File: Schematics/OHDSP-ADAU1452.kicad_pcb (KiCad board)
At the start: 4 copper layers, 100 x 100 mm, 308 parts, among them CN201 COAX, CN401 COAX, CN402 COAX, CN405 COAX, CN406 COAX, P201 CONN_2x1, P202 CONN_2x1, P203 CONN_6X2, P204 CONN_6x1, P301 CONN_2x1, P302 CONN_2x1, P303 PIN, P304 PIN, P305 PIN, P306 PIN, P601 CONN_02X05, P602 CONN_02X05, P603 CONN_02X05, P604 CONN_02X05, P605 CONN_3x1, P606 CONN_6X2, P607 CONN_02X05, P608 CONN_02X05, P609 CONN_02X20, P610 CONN_02X05, P611 CONN_5x1, P613 CONN_02X05, P614 CONN_02X05, P615 CONN_02X05, P616 CONN_02X05, SW201 SWITCH, SW202 SWITCH, U201 ADAU1452WBCPZ, U202 ADM13307-5ARZ, U203 25AA1024, U301 IC-REG-XRP7659ISTR-F, U302 IC-REG-XRP7659ISTR-F, U304 IC-REG-XC6210B332MR, U305 IC-REG-XC6210B332MR, U401 NB3L553, U501 IC-SPDIF-RX-OPTO, U502 IC-SPDIF-TX-OPTO, X201 24M576

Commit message: PCB work
More pcb work, some footprint changes, previous commit also had some
minor footprint changes and 0R resistors added...
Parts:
- C239, C240, C243, C245, L204, L205, R228, R234: moved to B.Cu
- moved L205 438.1 mm to (233.7, 130.3)
- moved C240 426.7 mm to (239.5, 136.1), turned to 90 degrees
- moved L204 423.6 mm to (233.7, 137.7)
- moved C245 363.9 mm to (233.7, 132.8), turned to 180 degrees
- moved C239 353.0 mm to (233.7, 135.1), turned to 180 degrees
- moved R228 301.5 mm to (237.0, 136.1), turned to 90 degrees
- moved R234 295.6 mm to (237.0, 131.8), turned to 270 degrees
- moved C227 16.7 mm to (273.3, 99.1), turned to 0 degrees
- moved C243 15.6 mm to (239.5, 131.8), turned to 270 degrees
- moved C224 15.6 mm to (276.4, 102.1), turned to 90 degrees
- moved R225 15.3 mm to (275.6, 105.2)
- moved C225 15.1 mm to (273.3, 103.1), turned to 0 degrees
- moved C226 15.1 mm to (273.3, 101.1), turned to 0 degrees
- moved L203 11.8 mm to (271.0, 105.2), turned to 0 degrees
- moved C228 2.90 mm to (276.6, 88.1), turned to 180 degrees
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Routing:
- net /ADAU1452/DVDD: track 78.3 -> 93.8 mm, vias 1 -> 2
- net VPP: track 32.9 -> 37.6 mm
- net /ADAU1452/IOVDD: track 78.1 -> 78.3 mm, vias 1 -> 2

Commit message: PCB work, footprint changes
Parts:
- C239, C240, C243, C245, L204, L205, R228, R234: moved to F.Cu
- R217: footprint OHDSP-Footprints-Pretty:SMD-0805 -> OHDSP-Footprints-Pretty:SMD-0603
- R601, R602, R603, R634, R646, R647: moved to B.Cu
- moved C245 72.2 mm to (278.1, 75.9), turned to 270 degrees
- moved R234 68.4 mm to (275.3, 75.2), turned to 0 degrees
- moved L204 66.9 mm to (261.9, 77.0), turned to 270 degrees
- moved L205 66.9 mm to (271.5, 75.2)
- moved C243 65.5 mm to (275.3, 77.0), turned to 0 degrees
- moved R228 60.2 mm to (260.1, 80.5), turned to 180 degrees
- moved C240 59.4 mm to (262.9, 81.5), turned to 270 degrees
- moved C239 59.1 mm to (260.1, 82.3), turned to 0 degrees
- moved R603 22.4 mm to (294.9, 74.9)
- moved R602 21.6 mm to (297.4, 74.7)
- moved L203 18.8 mm to (252.7, 101.2)
- moved C225 18.1 mm to (255.7, 98.9)
- moved C241 17.0 mm to (286.2, 81.8)
- moved C226 16.6 mm to (256.7, 102.3)
- moved C250 16.2 mm to (289.1, 81.6)
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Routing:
- net /ADAU1452/IOVDD: track 78.3 -> 12.6 mm, vias 2 -> 0
- net VAA: track 0.00 -> 44.2 mm
- net VPP: track 37.6 -> 0.00 mm, vias 1 -> 0
- net (no net): track 23.4 -> 56.3 mm, vias 0 -> 1
- net /ADAU1452/DVDD: track 93.8 -> 68.5 mm, vias 2 -> 1
- net /ADAU1452/PVDD: track 6.94 -> 17.1 mm
- net /ADAU1452/AVDD: track 4.87 -> 13.0 mm
- net VDD: track 41.7 -> 48.6 mm
- net Net-(P609-Pad40): track 5.35 -> 0.00 mm
- net Net-(P609-Pad38): track 5.18 -> 0.00 mm
- net Net-(P609-Pad35): track 2.85 -> 0.03 mm
- net Net-(C221-Pad2): track 0.00 -> 1.52 mm
- net Net-(P609-Pad19): track 6.00 -> 4.85 mm

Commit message: PCB changes, minor schematic changes
Removed switch on selfboot pin, as it has a jumper anyway... Removed
SPI/I2C jumper for selfboot as sticking with serial EEPROM. Changed some
component footprints (R207 to R216 0603 to 0805).
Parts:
- removed C202: 100n, OHDSP-Footprints-Pretty:SMD-0805
- removed C248: 220u, OHDSP-Footprints-Pretty:CAP-TH-D6.3mmP2.5mm
- removed P202: CONN_2x1, OHDSP-Footprints-Pretty:CONN_SIL_2
- removed SW201: SWITCH, OHDSP-Footprints-Pretty:SW_TACT_TH
- R205: value 1k -> N/F
- R207, R208, R209, R210, R211, R212, R213, R214, R215, R216: footprint OHDSP-Footprints-Pretty:SMD-0603 -> OHDSP-Footprints-Pretty:SMD-0805
- R644: moved to B.Cu
- moved P201 471.7 mm to (259.7, 99.1), turned to 270 degrees
- moved R201 448.8 mm to (257.2, 101.3), turned to 90 degrees
- moved R216 43.4 mm to (253.5, 91.9)
- moved R211 43.4 mm to (257.3, 91.9)
- moved R214 41.6 mm to (248.2, 93.0)
- moved C226 37.9 mm to (284.0, 128.7)
- moved R215 37.6 mm to (251.5, 93.0), turned to 270 degrees
- moved R212 37.4 mm to (255.4, 93.0), turned to 270 degrees
- moved R213 36.3 mm to (248.2, 95.2)
- moved L203 35.3 mm to (276.5, 127.3)
- moved C227 35.1 mm to (276.6, 130.8)
- moved C225 34.4 mm to (270.1, 130.0)
- moved P610 17.6 mm to (240.0, 98.0), turned to 180 degrees
- moved R209 17.3 mm to (248.5, 104.5), turned to 0 degrees
- moved R210 13.0 mm to (248.5, 106.6)
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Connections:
- R205 pad 1: Net-(P202-Pad2) -> /ADAU1452/SS_M/MP0
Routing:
- net /ADAU1452/DVDD: track 68.5 -> 19.4 mm
- net Net-(P609-Pad24): track 0.00 -> 28.3 mm
- net Net-(P609-Pad19): track 4.85 -> 20.5 mm
- net Net-(R212-Pad2): track 6.53 -> 21.9 mm
- net Net-(P609-Pad21): track 16.3 -> 30.5 mm
- net Net-(R207-Pad2): track 10.9 -> 23.8 mm
- net /ADAU1452/SPI_MOSI: track 4.66 -> 17.3 mm
- net /ADAU1452/SELFBOOT: track 0.00 -> 12.4 mm
- net Net-(R211-Pad2): track 7.38 -> 19.5 mm
- net /ADAU1452/SPI_MISO: track 26.3 -> 16.7 mm
- net /ADAU1452/I2C_SCL: track 72.1 -> 63.2 mm
- net Net-(R209-Pad2): track 15.7 -> 24.0 mm
- net Net-(P607-Pad7): track 28.0 -> 21.3 mm
- net /ADAU1452/M_SS: track 47.4 -> 53.2 mm
- net /ADAU1452/XTALIN: track 26.0 -> 20.3 mm
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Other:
- rule trace_min: 0.25 -> 0.2

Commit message: PCB Work
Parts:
- added C202: 220u, OHDSP-Footprints-Pretty:CAP-TH-D6.3mmP2.5mm, F.Cu at (255.0, 81.0)
- moved L203 30.7 mm to (254.1, 106.2)
- moved R601 9.41 mm to (300.7, 76.7)
- moved R634 9.14 mm to (281.9, 76.6)
- moved R603 4.50 mm to (290.6, 76.2)
- moved R646 0.77 mm to (276.2, 75.8), turned to 270 degrees
- moved C507 0.51 mm to (288.0, 71.1)
- moved R647 0.40 mm to (278.6, 75.7), turned to 270 degrees
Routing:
- net (no net): track 56.3 -> 23.4 mm, vias 1 -> 0
- net /ADAU1452/ADAU_SPDIF_RX: track 19.8 -> 18.9 mm
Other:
- board text added: "Seeed Studio/Fusion PCB do a 1mm stackup that would give reasonable trace widths For 50ohm use inner layer as ground (5mil clearance), trace width is 0.24mm For 75ohm keep inner layers clear, bottom as ground, trace width is 0.5mm For 100ohm keep inner layers clear, bottom ground, use 0.25mm All are approximate..."

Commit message: PCB Work
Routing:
- net /ADAU1452/DACOUT_BCLK2: track 20.8 -> 13.9 mm
- net /ADAU1452/DACOUT_SDATA2: track 18.0 -> 11.8 mm

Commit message: PCB work, removed a cap
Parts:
- removed C402: 220u, OHDSP-Footprints-Pretty:CAP-TH-D6.3mmP2.5mm
- C321, C503, C504, C505, C506, R231, R502: moved to B.Cu
- moved C506 651.2 mm to (300.5, 61.5), turned to 180 degrees
- moved R502 649.4 mm to (297.9, 65.8), turned to 180 degrees
- moved C505 633.9 mm to (282.4, 61.5), turned to 180 degrees
- moved C503 630.3 mm to (277.6, 61.0), turned to 90 degrees
- moved C504 624.5 mm to (272.5, 61.0), turned to 90 degrees
- moved R501 621.8 mm to (270.3, 61.0), turned to 90 degrees
- moved C501 619.2 mm to (267.2, 59.9), turned to 180 degrees
- moved L501 618.4 mm to (267.2, 62.5)
- moved C502 599.5 mm to (275.1, 61.0), turned to 90 degrees
- moved C401 387.7 mm to (258.1, 107.2), turned to 270 degrees
- moved C403 385.6 mm to (255.1, 108.2)
- moved C404 383.4 mm to (252.7, 115.4), turned to 180 degrees
- moved L401 377.8 mm to (252.3, 105.0), turned to 270 degrees
- moved R401 370.8 mm to (255.3, 106.0)
- moved C225 47.4 mm to (269.0, 82.7)
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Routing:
- net /ADAU1452/DVDD: track 19.4 -> 87.7 mm, vias 1 -> 2
- net VPP: track 0.00 -> 59.5 mm, vias 0 -> 1
- net /ADAU1452/IOVDD: track 15.9 -> 73.2 mm, vias 0 -> 3
- net Net-(C502-Pad1): track 0.00 -> 47.1 mm
- net Net-(C315-Pad1): track 6.70 -> 46.1 mm, vias 0 -> 1
- net VDD: track 43.4 -> 72.5 mm, vias 1 -> 2
- net Net-(C252-Pad1): track 0.00 -> 26.5 mm
- net VAA: track 49.0 -> 69.6 mm
- net /ADAU1452/EE_~CS: track 3.00 -> 22.3 mm
- net Net-(C403-Pad1): track 0.00 -> 14.5 mm
- net /ADAU1452/EE_SCK: track 1.91 -> 16.0 mm
- net /ADAU1452/EE_SI: track 0.00 -> 14.1 mm
- net Net-(C321-Pad1): track 0.00 -> 12.4 mm, vias 0 -> 1
- net /Connectors/RPI_BCLK: track 28.4 -> 39.4 mm
- net Net-(C309-Pad2): track 0.00 -> 9.05 mm
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
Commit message: PCB Work
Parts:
- moved SW202 93.0 mm to (276.5, 128.3)
- moved C231 73.3 mm to (259.7, 112.0), turned to 90 degrees
- moved R233 69.3 mm to (259.0, 115.0), turned to 0 degrees
- moved R226 61.8 mm to (252.3, 110.6)
- moved L202 61.6 mm to (250.9, 118.5)
- moved C218 61.2 mm to (255.2, 118.5), turned to 0 degrees
- moved R206 61.1 mm to (254.1, 121.8), turned to 270 degrees
- moved C214 57.2 mm to (250.9, 122.8), turned to 180 degrees
- moved U202 55.0 mm to (250.3, 116.2), turned to 0 degrees
- moved C216 49.2 mm to (250.9, 120.6), turned to 180 degrees
- moved R223 48.8 mm to (248.0, 113.8), turned to 270 degrees
- moved R222 48.8 mm to (246.1, 117.3), turned to 90 degrees
- moved R220 46.2 mm to (246.0, 109.5)
- moved R224 45.7 mm to (248.5, 110.6)
- moved R219 45.0 mm to (244.7, 113.4)
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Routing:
- net VDD: track 72.5 -> 133.1 mm, vias 2 -> 3
- net VPP: track 59.5 -> 86.4 mm, vias 1 -> 2
- net VAA: track 69.6 -> 85.4 mm, vias 0 -> 1
- net Net-(C310-Pad2): track 0.00 -> 10.2 mm
- net Net-(C315-Pad1): track 46.1 -> 56.2 mm
- net Net-(C216-Pad1): track 0.00 -> 8.77 mm
- net +5V: track 0.00 -> 7.66 mm
- net Net-(D301-Pad2): track 0.00 -> 6.89 mm
- net Net-(P609-Pad2): track 0.00 -> 5.51 mm
- net Net-(C310-Pad1): track 0.00 -> 3.91 mm
- net Net-(C330-Pad1): track 0.00 -> 3.90 mm
- net Net-(D302-Pad1): track 0.00 -> 3.56 mm
- net Net-(C331-Pad1): track 0.00 -> 3.26 mm
- net Net-(R220-Pad2): track 11.2 -> 8.12 mm
- net /ADAU1452/DVDD: track 87.7 -> 90.7 mm, vias 2 -> 3
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
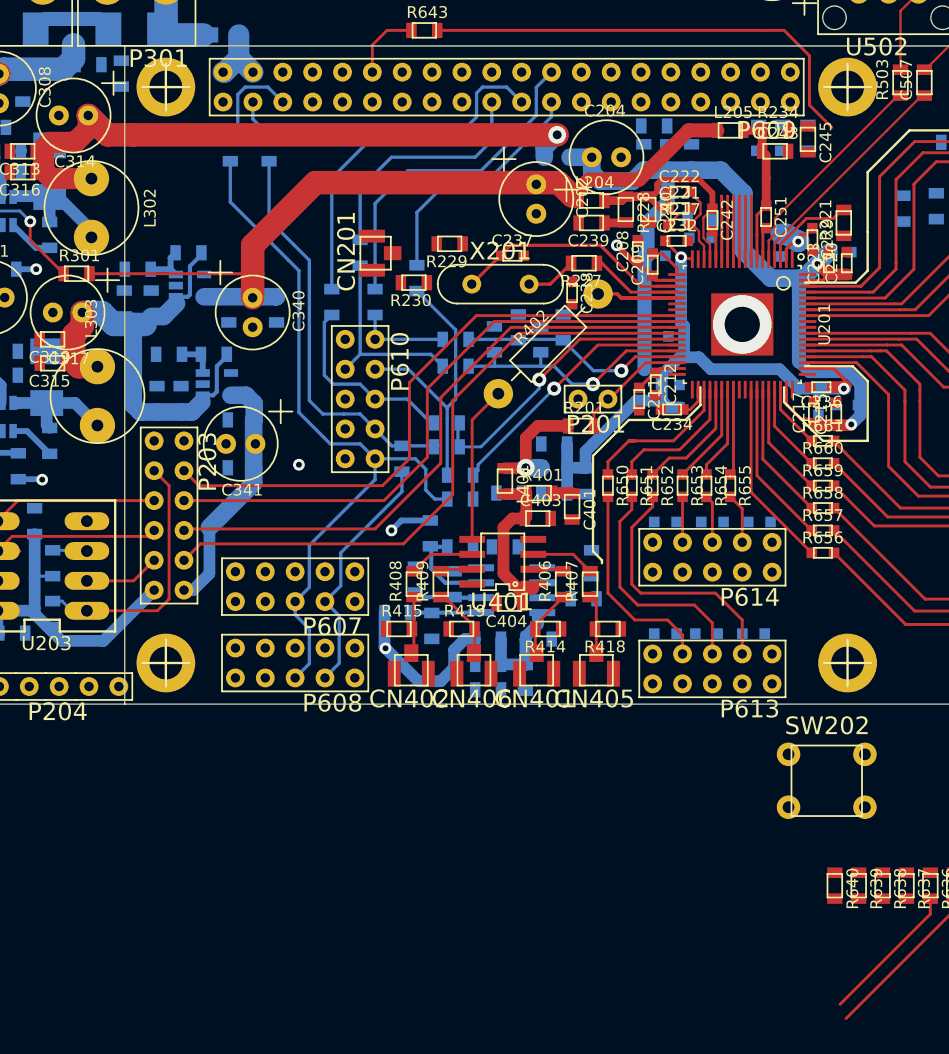
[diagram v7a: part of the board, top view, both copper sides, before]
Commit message: PCB Work, change reset switch to SMD
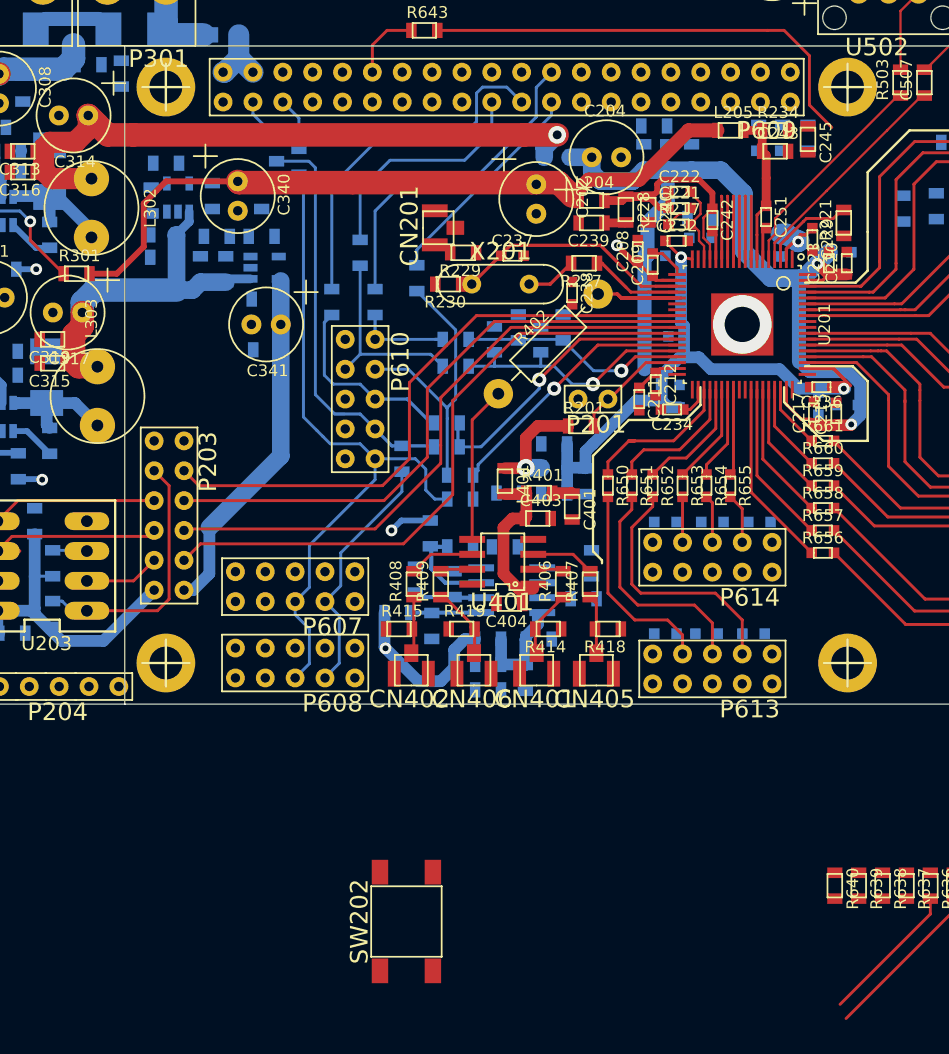
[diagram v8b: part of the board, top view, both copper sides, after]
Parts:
- SW202: footprint OHDSP-Footprints-Pretty:SW_TACT_TH -> OHDSP-Footprints-Pretty:SW_TACT_SMD
- moved SW202 35.5 mm to (244.0, 142.5)
- moved C326 12.5 mm to (228.6, 87.0)
- moved C329 11.2 mm to (226.4, 87.0)
- moved C331 10.8 mm to (227.8, 84.2)
- moved R314 10.8 mm to (231.6, 84.2)
- moved U305 10.7 mm to (231.9, 86.9)
- moved C335 10.5 mm to (231.9, 89.5)
- moved C341 10.4 mm to (232.0, 91.7)
- moved C338 10.3 mm to (232.0, 93.9)
- moved C340 9.99 mm to (229.6, 80.8)
- moved C334 9.75 mm to (227.5, 80.8)
- moved C337 9.74 mm to (231.6, 80.8)
- moved R313 7.85 mm to (223.5, 78.0)
- moved U304 7.56 mm to (224.5, 80.9), turned to 180 degrees
- moved R630 5.95 mm to (234.8, 77.9)
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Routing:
- net VAA: track 85.4 -> 61.7 mm, vias 1 -> 0
- net VPP: track 86.4 -> 101.5 mm
- net Net-(C315-Pad1): track 56.2 -> 47.6 mm
- net Net-(C330-Pad1): track 3.90 -> 0.00 mm
- net Net-(P609-Pad5): track 8.36 -> 4.55 mm
- net /ADAU1452/I2C_SCL: track 63.2 -> 59.7 mm
- net Net-(C331-Pad1): track 3.26 -> 0.00 mm
- net Net-(P609-Pad23): track 21.3 -> 19.3 mm
- net /ADAU1452/I2C_SDA: track 34.4 -> 35.1 mm
